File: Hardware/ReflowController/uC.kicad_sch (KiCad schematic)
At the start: 20 parts

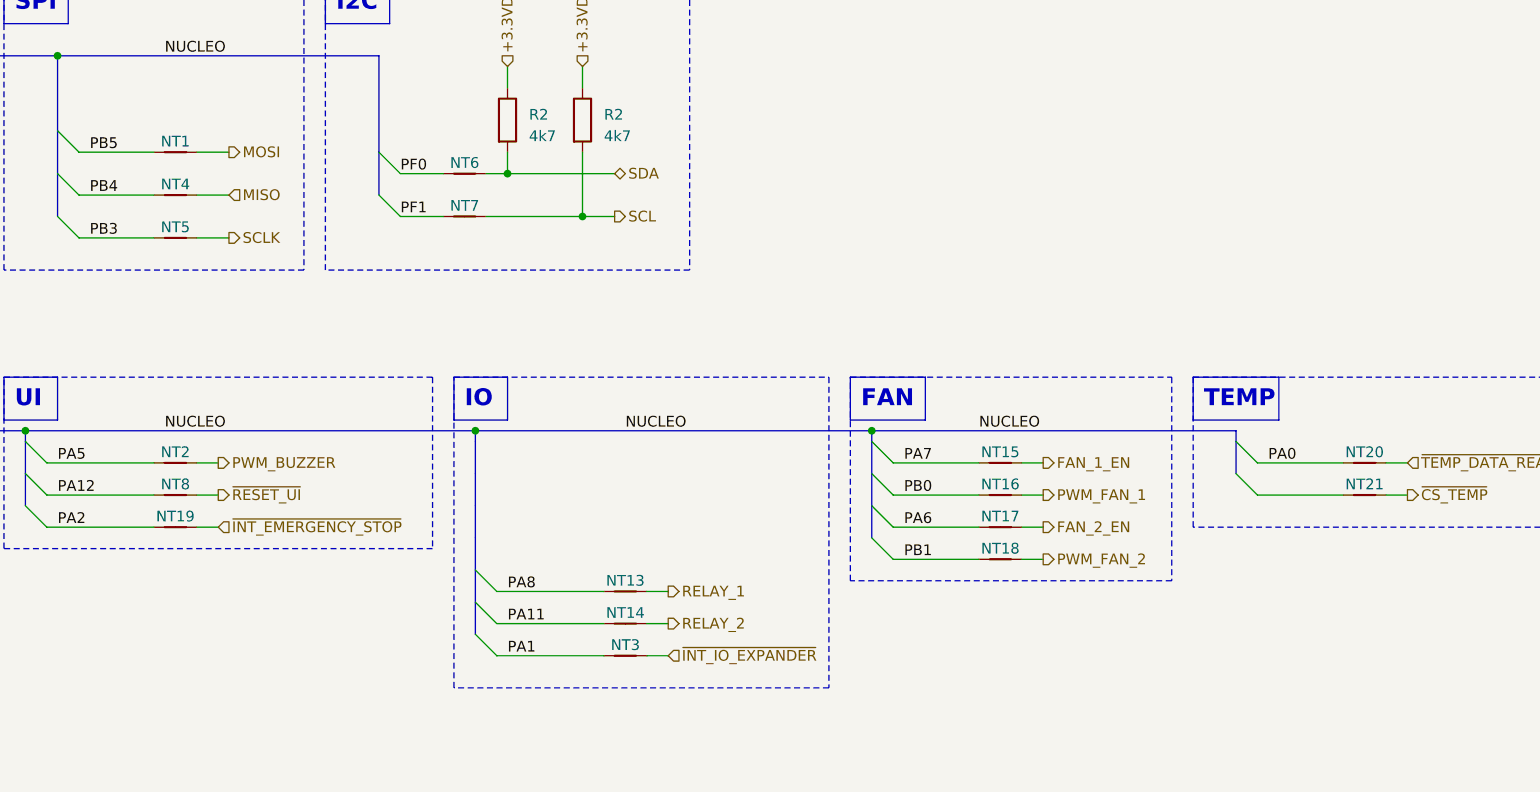
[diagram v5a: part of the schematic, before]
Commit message: work on porttable and on layout of temperature sensor
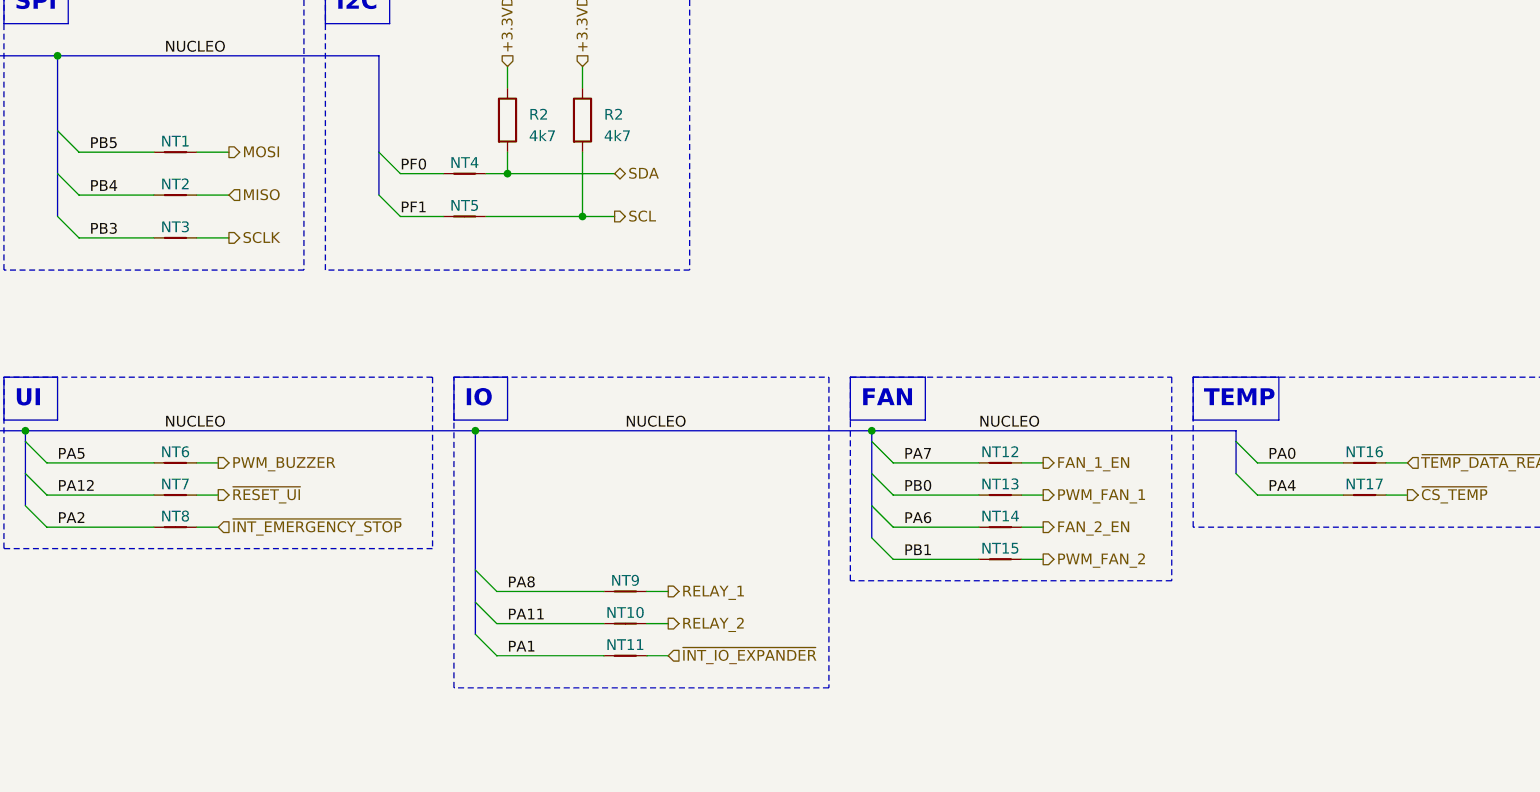
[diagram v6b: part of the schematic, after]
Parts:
- removed NT18, NT19, NT20, NT21: NetTie_2, symbol Device:NetTie_2
- added NT10, NT11, NT12, NT9: NetTie_2, NetTie:NetTie-2_SMD_Pad0.5mm, symbol Device:NetTie_2
- NT1, NT13, NT14, NT15, NT16, NT17, NT2, NT3, NT4, NT5, NT6, NT7, NT8: footprint (none) -> NetTie:NetTie-2_SMD_Pad0.5mm
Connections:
- net FAN_1_EN: now also NT12.2; no longer NT15.2
- net FAN_2_EN: now also NT14.2; no longer NT17.2
- net MISO: now also NT2.2; no longer NT4.2
- net PA0: now also NT16.1
- net PA1: now also NT11.1; no longer NT3.1
- net PA11: now also NT10.1; no longer NT14.1
- net PA12: now also NT7.1; no longer NT8.1
- net PA2: now also NT8.1
- net PA4: now also NT17.1
- net PA5: now also NT6.1; no longer NT2.1
- net PA6: now also NT14.1; no longer NT17.1
- net PA7: now also NT12.1; no longer NT15.1
- net PA8: now also NT9.1; no longer NT13.1
- net PB0: now also NT13.1; no longer NT16.1
- net PB1: now also NT15.1
- net PB3: now also NT3.1; no longer NT5.1
- net PB4: now also NT2.1; no longer NT4.1
- net PF0: now also NT4.1; no longer NT6.1
- net PF1: now also NT5.1; no longer NT7.1
- net PWM_BUZZER: now also NT6.2; no longer NT2.2
- net PWM_FAN_1: now also NT13.2; no longer NT16.2
- net PWM_FAN_2: now also NT15.2
- net RELAY_1: now also NT9.2; no longer NT13.2
- net RELAY_2: now also NT10.2; no longer NT14.2
- net SCL: now also NT5.2; no longer NT7.2
- net SCLK: now also NT3.2; no longer NT5.2
- net SDA: now also NT4.2; no longer NT6.2
- net ~{CS_TEMP}: now also NT17.2
- net ~{INT_EMERGENCY_STOP}: now also NT8.2
- net ~{INT_IO_EXPANDER}: now also NT11.2; no longer NT3.2
- net ~{RESET_UI}: now also NT7.2; no longer NT8.2
- net ~{TEMP_DATA_READY}: now also NT16.2

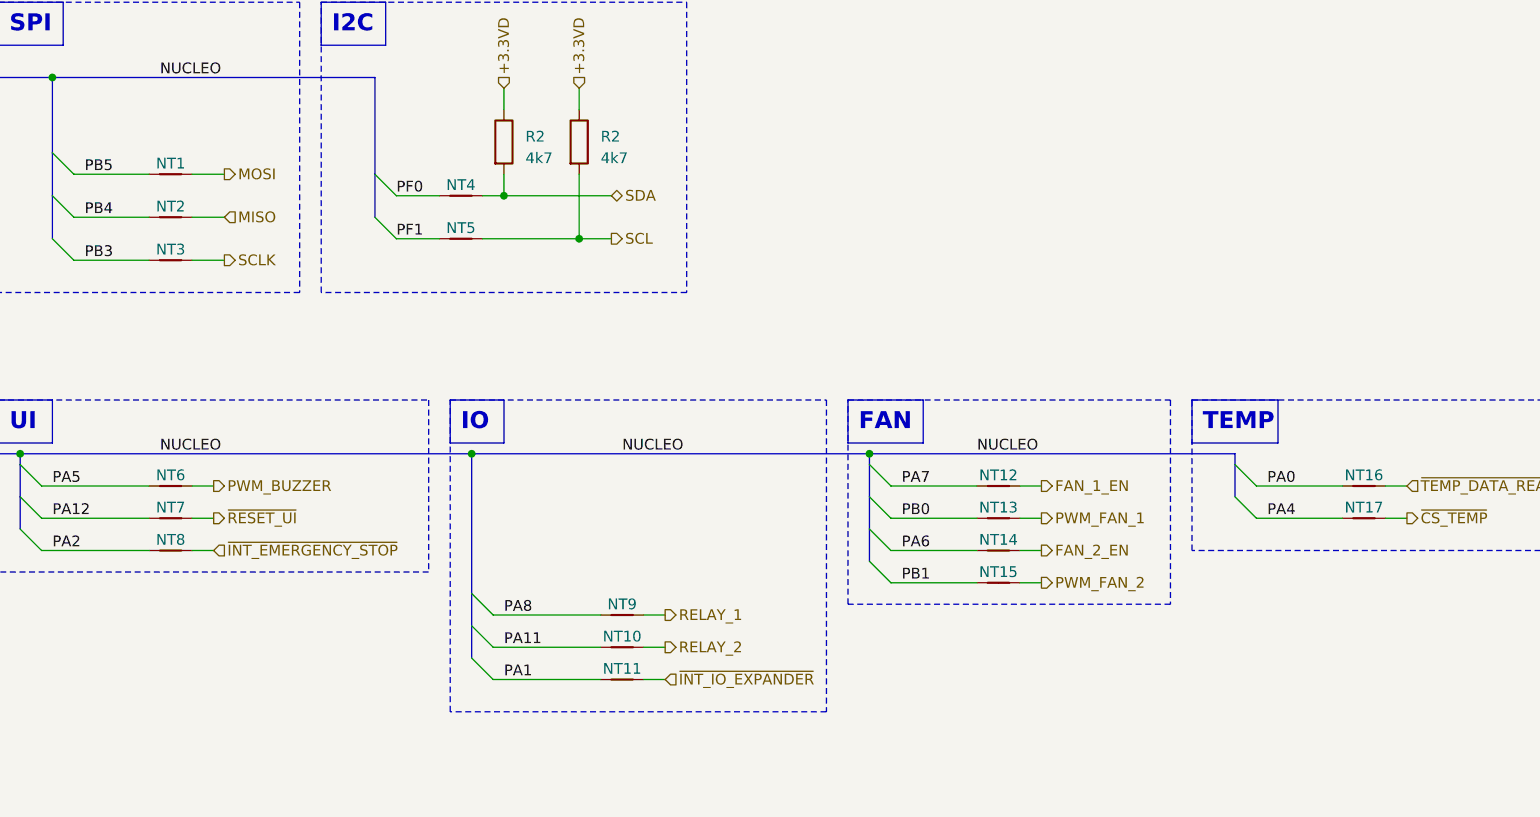
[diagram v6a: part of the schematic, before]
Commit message: Finished rewiev with Edwin, Need TO connect he HSS and DO the labeling
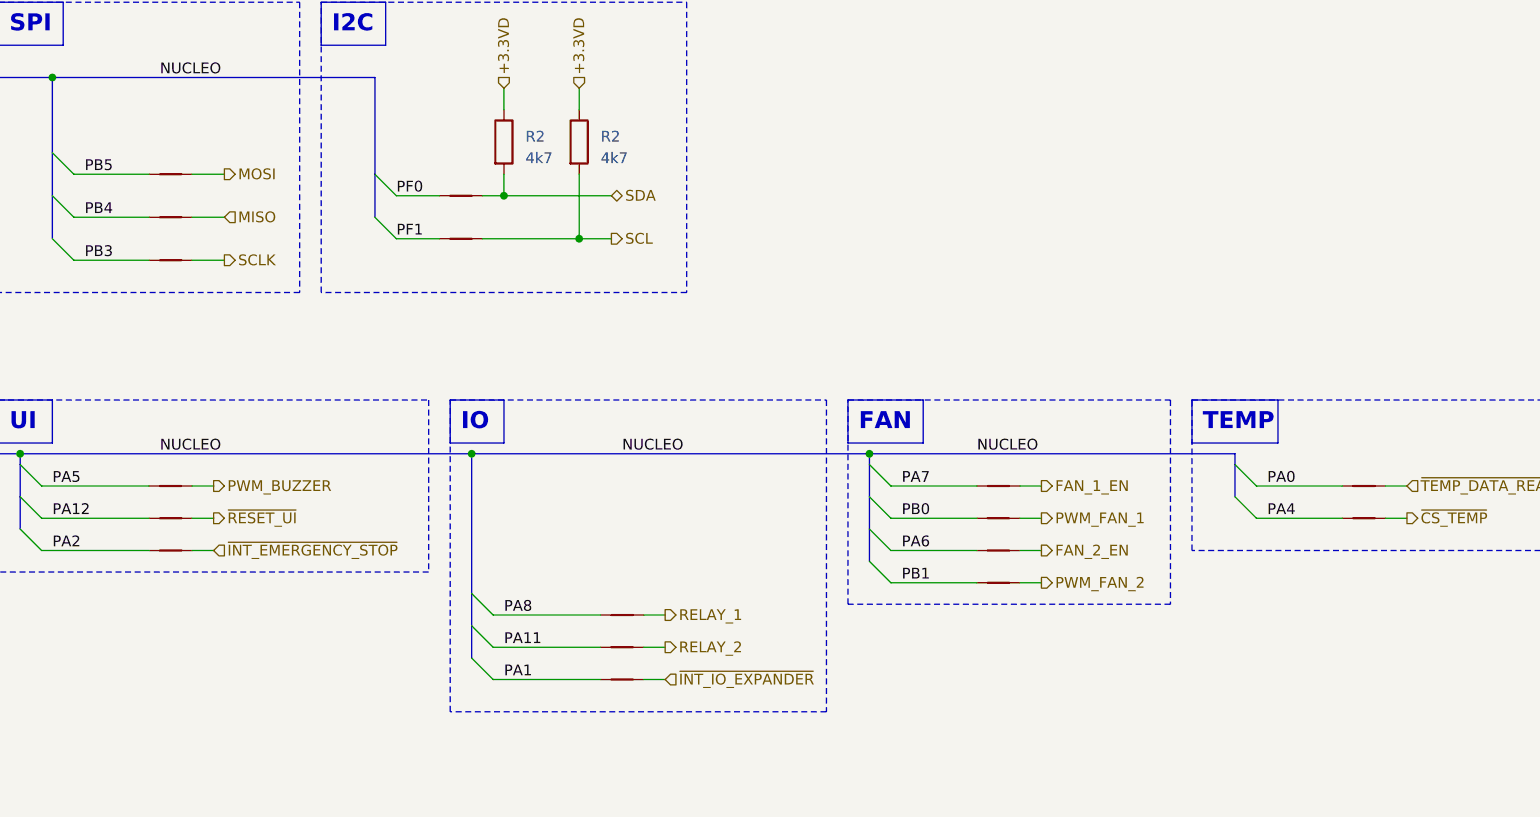
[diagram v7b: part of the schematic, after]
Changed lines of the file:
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@@
     (in_bom yes) (on_board yes) (dnp no)
     (property "Reference" "NT10" (at 168.91 129.54 0)
-      (effects (font (size 1.27 1.27)))
+      (effects (font (size 1.27 1.27)) hide)
     )
     (property "Value" "NetTie_2" (at 168.91 132.08 0)
@@
     (in_bom yes) (on_board yes) (dnp no)
     (property "Reference" "NT9" (at 168.91 125.73 0)
-      (effects (font (size 1.27 1.27)))
+      (effects (font (size 1.27 1.27)) hide)
     )
     (property "Value" "NetTie_2" (at 168.91 128.27 0)
@@
     (in_bom yes) (on_board yes) (dnp no)
     (property "Reference" "NT14" (at 213.36 118.11 0)
-      (effects (font (size 1.27 1.27)))
+      (effects (font (size 1.27 1.27)) hide)
     )
     (property "Value" "NetTie_2" (at 213.36 120.65 0)
@@
     (in_bom yes) (on_board yes) (dnp no)
     (property "Reference" "NT16" (at 256.54 110.49 0)
-      (effects (font (size 1.27 1.27)))
+      (effects (font (size 1.27 1.27)) hide)
     )
     (property "Value" "NetTie_2" (at 256.54 113.03 0)
@@
     (in_bom yes) (on_board yes) (dnp no)
     (property "Reference" "NT4" (at 149.86 76.2 0)
-      (effects (font (size 1.27 1.27)))
+      (effects (font (size 1.27 1.27)) hide)
     )
     (property "Value" "NetTie_2" (at 149.86 78.74 0)
@@
     (in_bom yes) (on_board yes) (dnp no)
     (property "Reference" "NT7" (at 115.57 114.3 0)
-      (effects (font (size 1.27 1.27)))
+      (effects (font (size 1.27 1.27)) hide)
     )
     (property "Value" "NetTie_2" (at 115.57 116.84 0)
@@
     (in_bom yes) (on_board yes) (dnp no)
     (property "Reference" "NT17" (at 256.54 114.3 0)
-      (effects (font (size 1.27 1.27)))
+      (effects (font (size 1.27 1.27)) hide)
     )
     (property "Value" "NetTie_2" (at 256.54 116.84 0)
@@
     (in_bom yes) (on_board yes) (dnp no)
     (property "Reference" "NT6" (at 115.57 110.49 0)
-      (effects (font (size 1.27 1.27)))
+      (effects (font (size 1.27 1.27)) hide)
     )
     (property "Value" "NetTie_2" (at 115.57 113.03 0)
@@
     (in_bom yes) (on_board yes) (dnp no)
     (property "Reference" "NT12" (at 213.36 110.49 0)
-      (effects (font (size 1.27 1.27)))
+      (effects (font (size 1.27 1.27)) hide)
     )
     (property "Value" "NetTie_2" (at 213.36 113.03 0)
@@
     (in_bom yes) (on_board yes) (dnp no)
     (property "Reference" "NT3" (at 115.57 83.82 0)
-      (effects (font (size 1.27 1.27)))
+      (effects (font (size 1.27 1.27)) hide)
     )
     (property "Value" "NetTie_2" (at 115.57 86.36 0)
@@
     (in_bom yes) (on_board yes) (dnp no)
     (property "Reference" "NT5" (at 149.86 81.28 0)
-      (effects (font (size 1.27 1.27)))
+      (effects (font (size 1.27 1.27)) hide)
     )
     (property "Value" "NetTie_2" (at 149.86 83.82 0)
@@
     (in_bom yes) (on_board yes) (dnp no)
     (property "Reference" "NT13" (at 213.36 114.3 0)
-      (effects (font (size 1.27 1.27)))
+      (effects (font (size 1.27 1.27)) hide)
     )
     (property "Value" "NetTie_2" (at 213.36 116.84 0)
@@
     (in_bom yes) (on_board yes) (dnp no)
     (property "Reference" "NT8" (at 115.57 118.11 0)
-      (effects (font (size 1.27 1.27)))
+      (effects (font (size 1.27 1.27)) hide)
     )
     (property "Value" "NetTie_2" (at 115.57 120.65 0)
@@
     (in_bom yes) (on_board yes) (dnp no)
     (property "Reference" "NT15" (at 213.36 121.92 0)
-      (effects (font (size 1.27 1.27)))
+      (effects (font (size 1.27 1.27)) hide)
     )
     (property "Value" "NetTie_2" (at 213.36 124.46 0)
@@
     (in_bom yes) (on_board yes) (dnp no)
     (property "Reference" "NT11" (at 168.91 133.35 0)
-      (effects (font (size 1.27 1.27)))
+      (effects (font (size 1.27 1.27)) hide)
     )
     (property "Value" "NetTie_2" (at 168.91 135.89 0)
@@
     (in_bom yes) (on_board yes) (dnp no)
     (property "Reference" "NT1" (at 115.57 73.66 0)
-      (effects (font (size 1.27 1.27)))
+      (effects (font (size 1.27 1.27)) hide)
     )
     (property "Value" "NetTie_2" (at 115.57 76.2 0)
@@
     (in_bom yes) (on_board yes) (dnp no)
     (property "Reference" "NT2" (at 115.57 78.74 0)
-      (effects (font (size 1.27 1.27)))
+      (effects (font (size 1.27 1.27)) hide)
     )
     (property "Value" "NetTie_2" (at 115.57 81.28 0)
